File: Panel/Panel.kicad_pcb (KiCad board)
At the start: 2 copper layers, 100 x 100 mm, 91 parts, among them J1 Conn_01x03, J10 Conn_01x02, J11 Conn_01x03, J12 Conn_01x03, J14 Conn_01x02, J15 Conn_01x02, J2 USB_C_Receptacle_USB2.0, J3 Conn_01x02, J4 Conn_02x06_Odd_Even, J5 Conn_01x07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

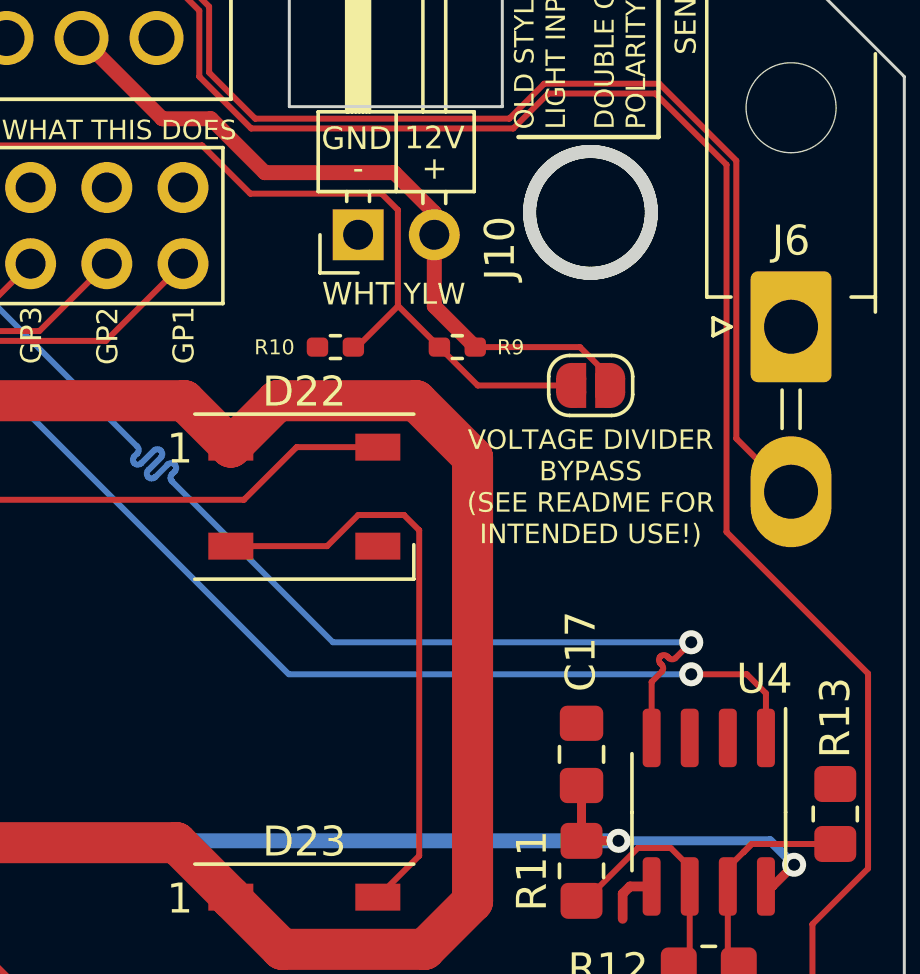
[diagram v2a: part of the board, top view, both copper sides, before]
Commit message: Fix an oopsie, control RE/DE via GPIO by default
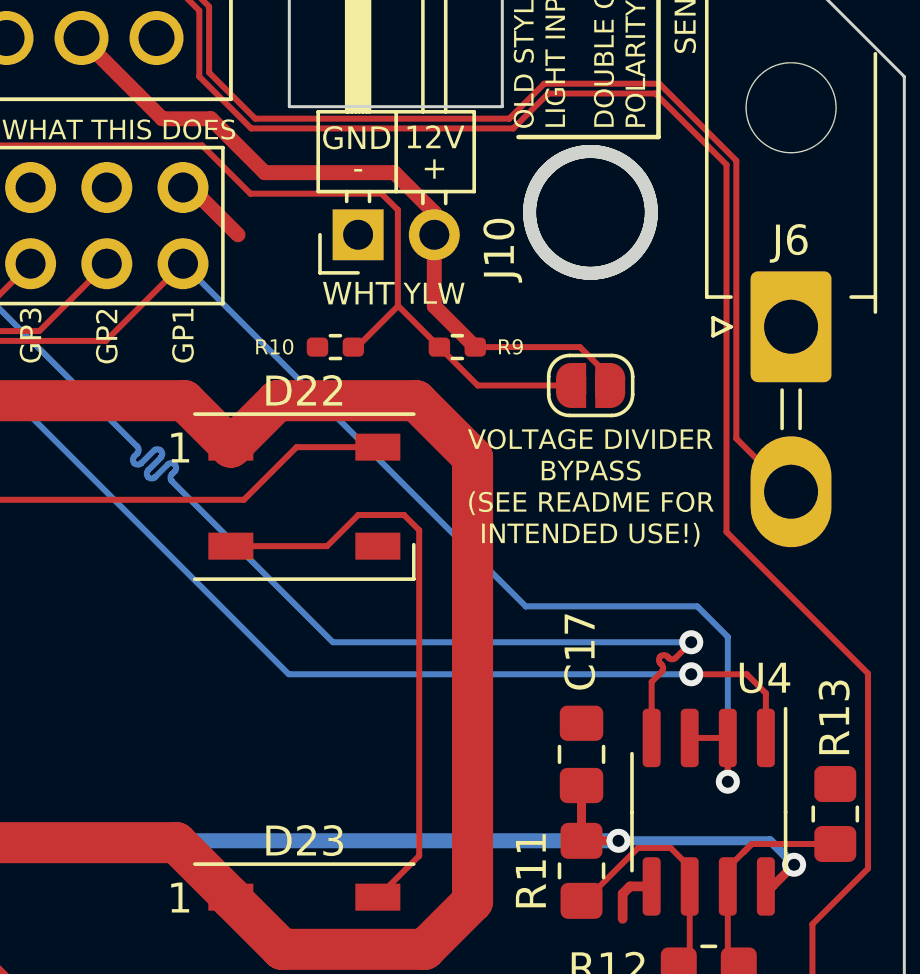
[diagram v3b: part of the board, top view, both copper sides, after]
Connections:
- U4 pad 2: GND -> GPIO1
- U4 pad 3: GND -> GPIO1
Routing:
- net GPIO1: track 56.1 -> 87.0 mm, vias 2 -> 3
- net GND: track 15.9 -> 18.4 mm
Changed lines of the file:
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@@
       (net 42 "GPIO5") (pinfunction "RO") (pintype "output"))
     (pad "2" smd roundrect (at -2.475 -0.635 270) (size 1.95 0.6) (layers "F.Cu" "F.Paste" "F.Mask") (roundrect_rratio 0.25)
-      (net 2 "GND") (pinfunction "~{RE}") (pintype "input"))
+      (net 38 "GPIO1") (pinfunction "~{RE}") (pintype "input"))
     (pad "3" smd roundrect (at -2.475 0.635 270) (size 1.95 0.6) (layers "F.Cu" "F.Paste" "F.Mask") (roundrect_rratio 0.25)
-      (net 2 "GND") (pinfunction "DE") (pintype "input"))
+      (net 38 "GPIO1") (pinfunction "DE") (pintype "input"))
     (pad "4" smd roundrect (at -2.475 1.905 270) (size 1.95 0.6) (layers "F.Cu" "F.Paste" "F.Mask") (roundrect_rratio 0.25)
       (net 41 "GPIO4") (pinfunction "DI") (pintype "input"))
@@
   (segment (start 118.3311 56.9976) (end 118.1608 57.1679) (width 0.3) (layer "F.Cu") (net 2))
   (segment (start 98.975 56.095) (end 98.975 54.745) (width 0.65) (layer "F.Cu") (net 2))
+  (segment (start 156.215 59.695) (end 157.791 61.271) (width 0.5) (layer "F.Cu") (net 2))
+  (segment (start 155.956 59.695) (end 156.215 59.695) (width 0.2) (layer "F.Cu") (net 2))
   (segment (start 118.1608 57.1679) (end 118.1608 58.5724) (width 0.3) (layer "F.Cu") (net 2))
   (segment (start 118.1608 58.5724) (end 118.0592 58.674) (width 0.3) (layer "F.Cu") (net 2))
@@
   (segment (start 126.713023 65.7775) (end 126.713023 64.827907) (width 0.2) (layer "F.Cu") (net 38))
   (segment (start 109.439972 63.211972) (end 109.439972 62.103) (width 0.2) (layer "F.Cu") (net 38))
+  (segment (start 174.117 79.502) (end 174.117 78.043) (width 0.2) (layer "F.Cu") (net 38))
+  (segment (start 172.847 78.043) (end 174.117 78.043) (width 0.2) (layer "F.Cu") (net 38))
   (segment (start 153.383 64.808) (end 155.956 62.235) (width 0.2) (layer "F.Cu") (net 38))
   (segment (start 126.713023 64.827907) (end 127.508 64.03293) (width 0.2) (layer "F.Cu") (net 38))
@@
   (segment (start 111.103739 65.7775) (end 111.103739 64.875739) (width 0.2) (layer "F.Cu") (net 38))
   (via (at 126.713023 65.7775) (size 0.8) (drill 0.4) (layers "F.Cu" "B.Cu") (net 38))
+  (via (at 174.117 79.502) (size 0.8) (drill 0.4) (layers "F.Cu" "B.Cu") (net 38))
   (via (at 111.103739 65.7775) (size 0.8) (drill 0.4) (layers "F.Cu" "B.Cu") (net 38))
   (segment (start 126.713023 65.7775) (end 126.086023 66.4045) (width 0.2) (layer "B.Cu") (net 38))
+  (segment (start 174.117 74.676) (end 174.117 79.502) (width 0.2) (layer "B.Cu") (net 38))
   (segment (start 126.086023 66.4045) (end 111.730739 66.4045) (width 0.2) (layer "B.Cu") (net 38))
+  (segment (start 173.101 73.66) (end 174.117 74.676) (width 0.2) (layer "B.Cu") (net 38))
   (segment (start 111.730739 66.4045) (end 111.103739 65.7775) (width 0.2) (layer "B.Cu") (net 38))
+  (segment (start 155.956 62.235) (end 167.381 73.66) (width 0.2) (layer "B.Cu") (net 38))
+  (segment (start 167.381 73.66) (end 173.101 73.66) (width 0.2) (layer "B.Cu") (net 38))
   (segment (start 112.030242 65.339794) (end 112.030242 65.7775) (width 0.2) (layer "F.Cu") (net 39))
   (segment (start 125.78652 65.7775) (end 125.78652 65.291962) (width 0.2) (layer "F.Cu") (net 39))

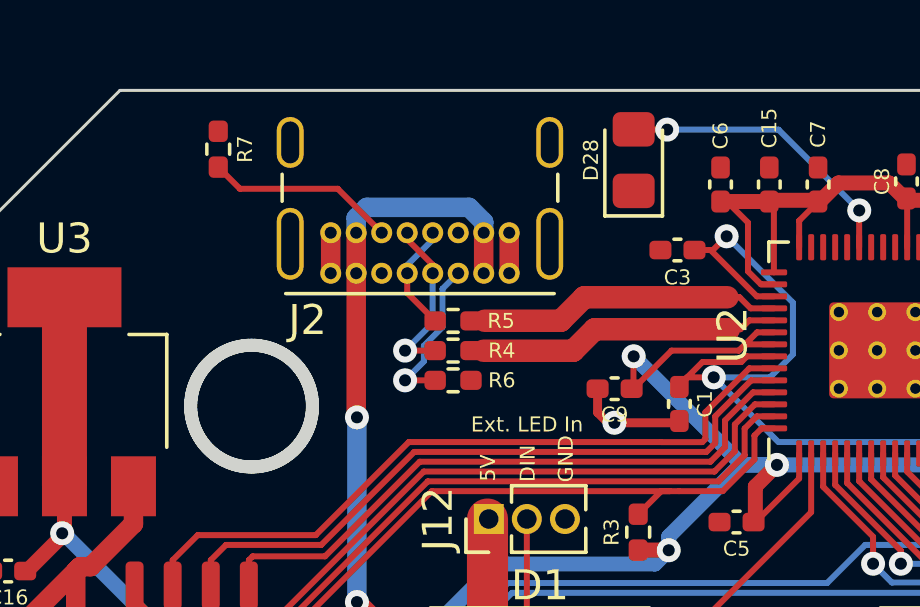
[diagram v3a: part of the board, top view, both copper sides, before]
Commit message: Replaced USB C port with cheaper alternative
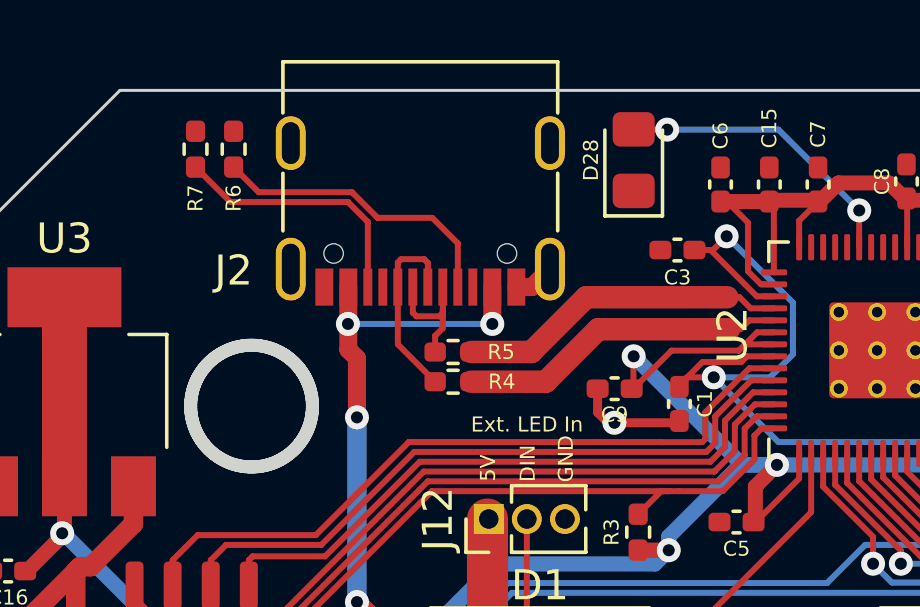
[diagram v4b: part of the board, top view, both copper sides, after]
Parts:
- J2: footprint Connector_USB:USB_C_Receptacle_GCT_USB4085 -> Connector_USB:USB_C_Receptacle_G-Switch_GT-USB-7010ASV
- moved R6 10.6 mm to (89.8, 52.0), turned to 90 degrees
- moved J2 4.41 mm to (96.0, 52.8)
- moved R4 1.04 mm to (97.1, 59.7)
- moved R5 1.04 mm to (97.1, 58.7)
- moved R7 0.76 mm to (88.5, 52.0)
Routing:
- net Net-(J2-CC1): track 5.31 -> 9.98 mm, vias 1 -> 0
- net Net-(F1-Pad1): track 22.3 -> 19.9 mm, vias 2 -> 4
- net Net-(J2-CC2): track 6.35 -> 8.67 mm
- net GND: track 18.4 -> 17.1 mm
- net USB D-: track 3.68 -> 4.47 mm
- net USB D+: track 5.67 -> 6.39 mm, vias 1 -> 0
